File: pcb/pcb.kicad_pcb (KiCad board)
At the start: 2 copper layers, 165.5 x 101.1 mm, 59 parts, among them J1 N!N, J2 Conn_01x02_Socket, J4 Display_nice-view, J8 Conn_01x12_Socket, J9 Conn_01x12_Socket, SW1 Switch, SW10 Switch, SW11 Switch, SW12 Switch, SW13 Switch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

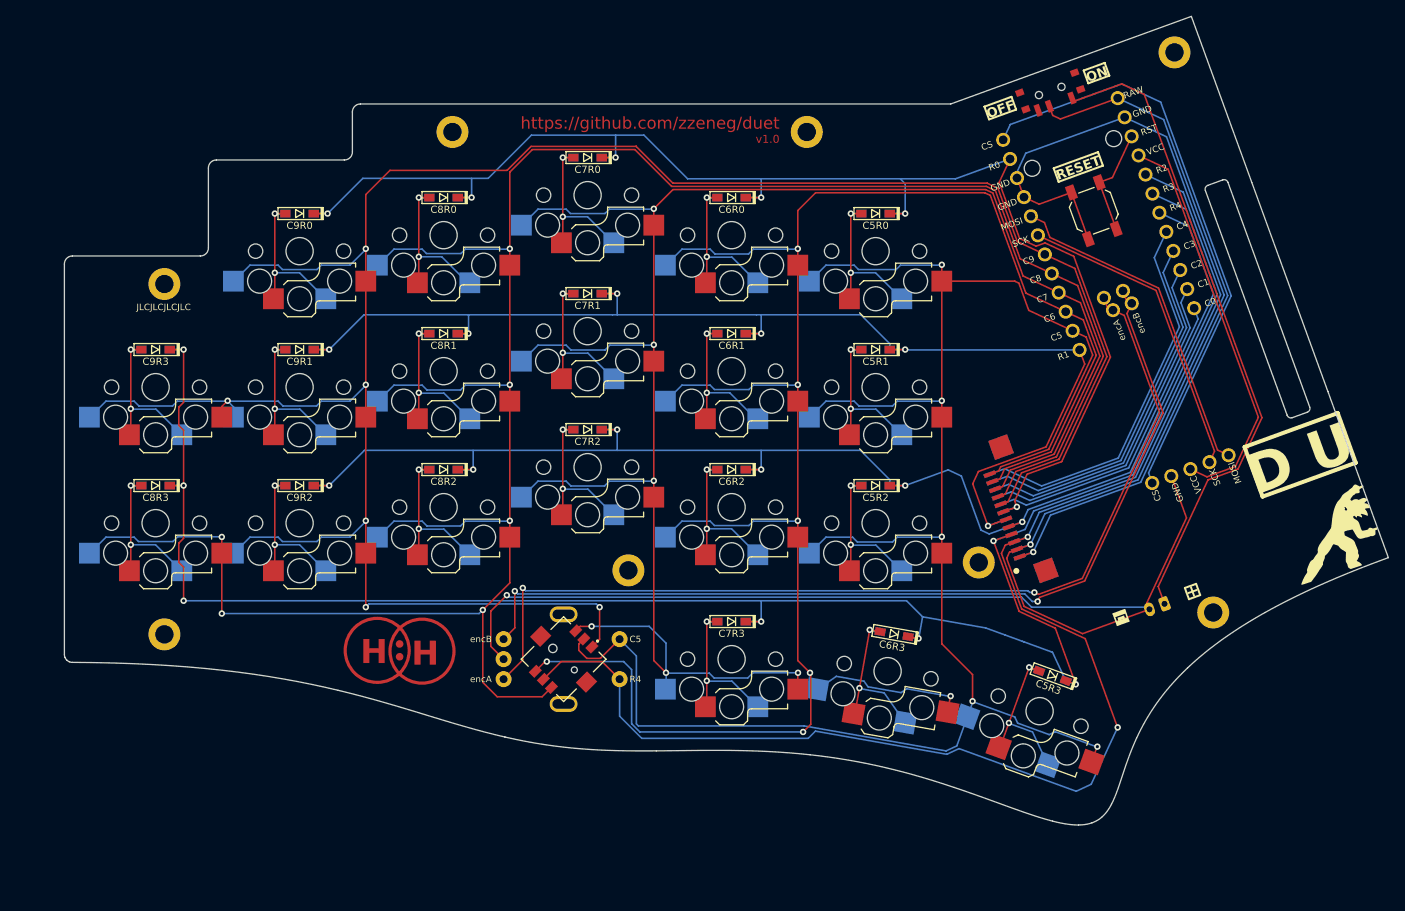
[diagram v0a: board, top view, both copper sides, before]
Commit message: converting duet to standard x and min y spacing, along with strong pinky stagger, WIP
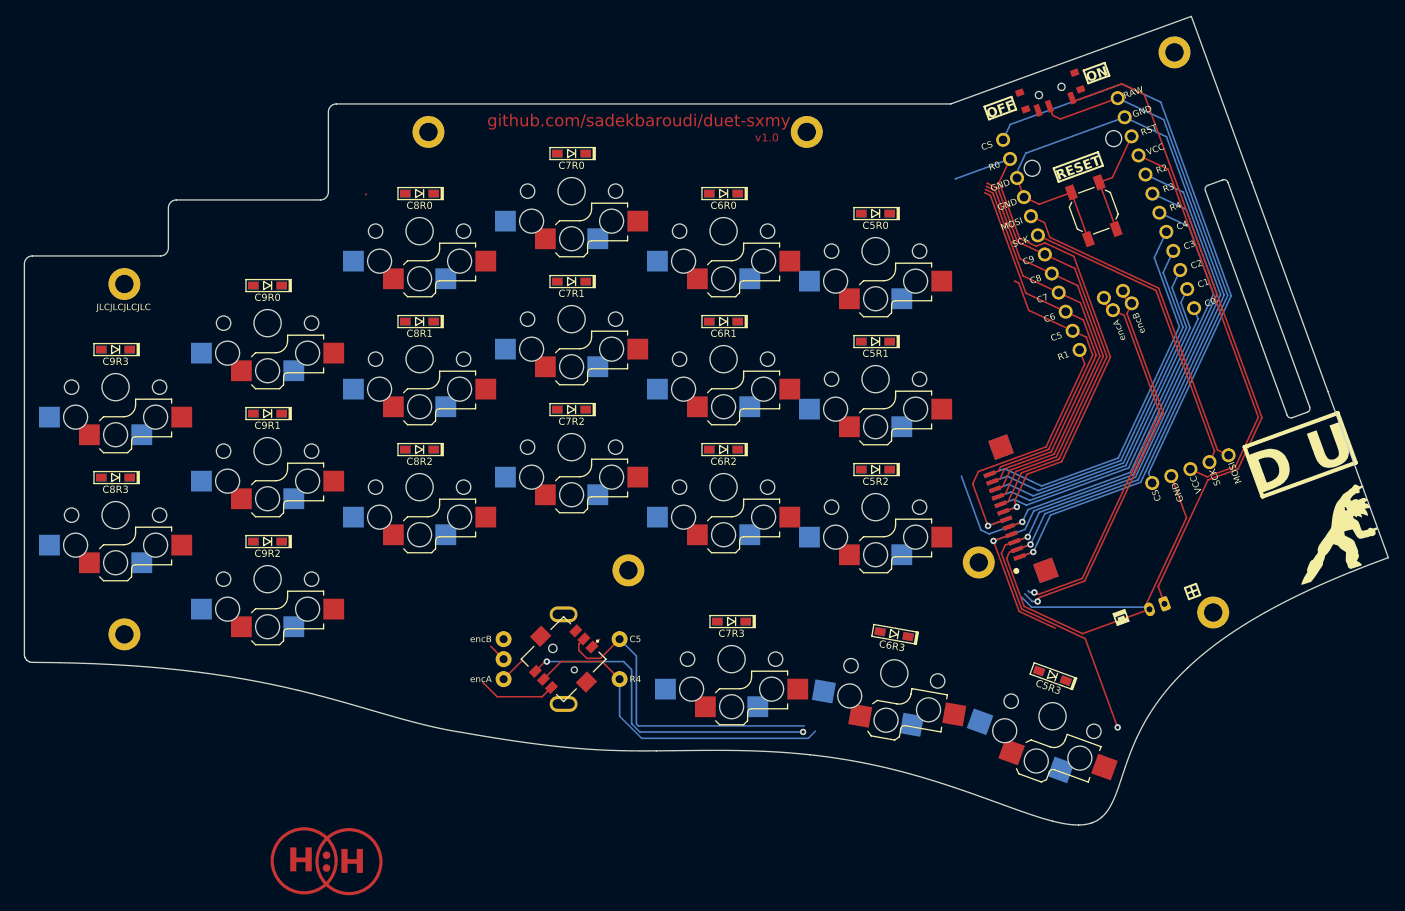
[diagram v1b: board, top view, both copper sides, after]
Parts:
- SW1, SW10, SW11, SW12, SW13, SW14, SW15, SW16, SW17, SW18, SW19, SW2, SW20, SW3, SW4, SW5, SW6, SW7, SW8, SW9: footprint zzkeeb:Switch_ChocV1-hotswap-reversible -> fingerpunch:Switch_ChocV1-hotswap-minY-reversible
- moved D1 9.85 mm to (61.5, 63.3)
- moved SW1 9.85 mm to (61.5, 68.0)
- moved D6 8.94 mm to (61.5, 79.3)
- moved SW6 8.94 mm to (61.5, 84.0)
- moved D11 8.06 mm to (61.5, 95.3)
- moved SW11 8.06 mm to (61.5, 100.0)
- moved D17 5.10 mm to (42.5, 87.3)
- moved SW17 5.10 mm to (42.5, 92.0)
- moved D16 5.00 mm to (42.5, 71.3)
- moved H1 5.00 mm to (43.6, 63.1)
- moved H5 5.00 mm to (43.6, 106.9)
- moved SW16 5.00 mm to (42.5, 76.0)
- moved D12 3.91 mm to (80.5, 83.8)
- moved SW12 3.91 mm to (80.5, 88.5)
- moved D7 3.35 mm to (80.5, 67.8)
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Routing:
- net col9: track 300.2 -> 53.8 mm, vias 6 -> 0
- net col8: track 302.5 -> 60.8 mm, vias 6 -> 0
- net col7: track 241.7 -> 49.7 mm, vias 6 -> 0
- net row3: track 253.0 -> 77.6 mm, vias 7 -> 1
- net col6: track 256.5 -> 89.9 mm, vias 7 -> 2
- net col5: track 240.3 -> 76.8 mm, vias 5 -> 0
- net row1: track 155.6 -> 34.4 mm, vias 6 -> 1
- net row0: track 180.7 -> 65.9 mm, vias 6 -> 1
- net row2: track 175.7 -> 67.5 mm, vias 6 -> 1
- net encA: track 122.4 -> 50.1 mm, vias 2 -> 1
- net GND: track 238.1 -> 166.5 mm, vias 2 -> 1
- net encB: track 118.9 -> 48.4 mm, vias 2 -> 1
- net row4: track 180.0 -> 136.1 mm
- net Net-(D3-A): track 21.2 -> 0.00 mm, vias 2 -> 0
- net Net-(D14-A): track 21.1 -> 0.00 mm, vias 2 -> 0
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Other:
- board size 165.5 x 101.1 mm -> 170.5 x 101.1 mm
- board text added: "-0.5"
- board text added: "10"
- board text added: "github.com/sadekbaroudi/duet-sxmy"
- board text removed: "https://github.com/zzeneg/duet"

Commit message: rerouted with the new layout, ready for production test
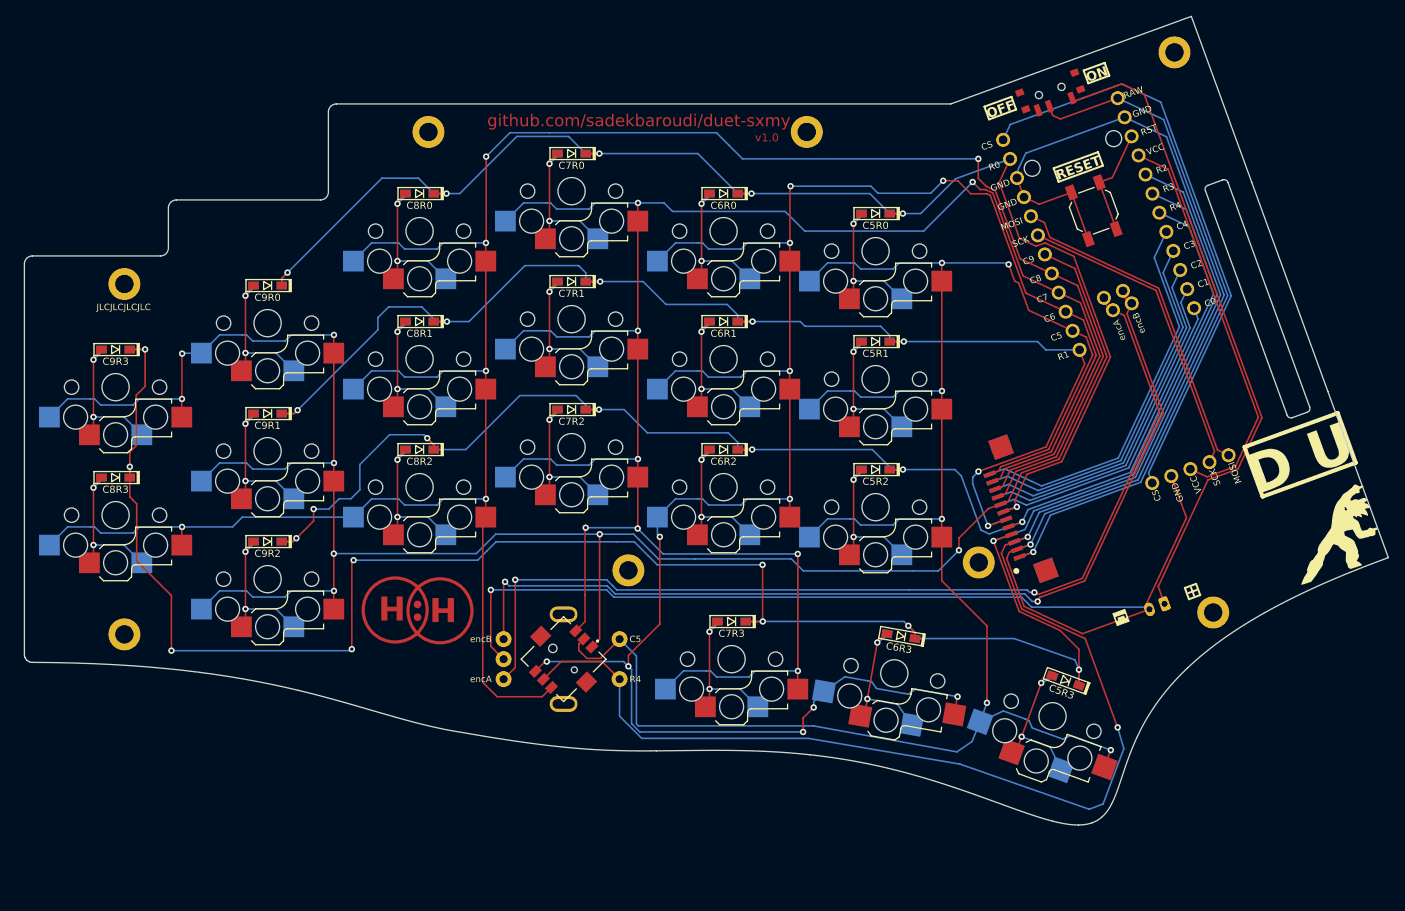
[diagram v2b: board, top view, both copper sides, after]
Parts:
- moved D20 1.75 mm to (161.3, 112.7)
- moved D19 0.90 mm to (140.7, 107.1)
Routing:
- net col8: track 60.8 -> 291.5 mm, vias 0 -> 6
- net col7: track 49.7 -> 269.1 mm, vias 0 -> 8
- net col9: track 53.8 -> 262.3 mm, vias 0 -> 8
- net row3: track 77.6 -> 276.4 mm, vias 1 -> 10
- net col5: track 76.8 -> 246.2 mm, vias 0 -> 6
- net col6: track 89.9 -> 258.7 mm, vias 2 -> 11
- net row1: track 34.4 -> 159.7 mm, vias 1 -> 7
- net row2: track 67.5 -> 178.6 mm, vias 1 -> 7
- net row0: track 65.9 -> 174.3 mm, vias 1 -> 6
- net encA: track 50.1 -> 124.4 mm, vias 1 -> 2
- net GND: track 166.5 -> 240.2 mm, vias 1 -> 2
- net encB: track 48.4 -> 121.3 mm, vias 1 -> 2
- net row4: track 136.1 -> 183.2 mm
- net Net-(D15-A): track 0.00 -> 19.9 mm, vias 0 -> 2
- net Net-(D9-A): track 0.00 -> 19.9 mm, vias 0 -> 2
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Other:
- board text removed: "-0.5"
- board text removed: "10"

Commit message: moved mounting hole, added updated dxfs, added sxmy cases, still need to do bottom plates
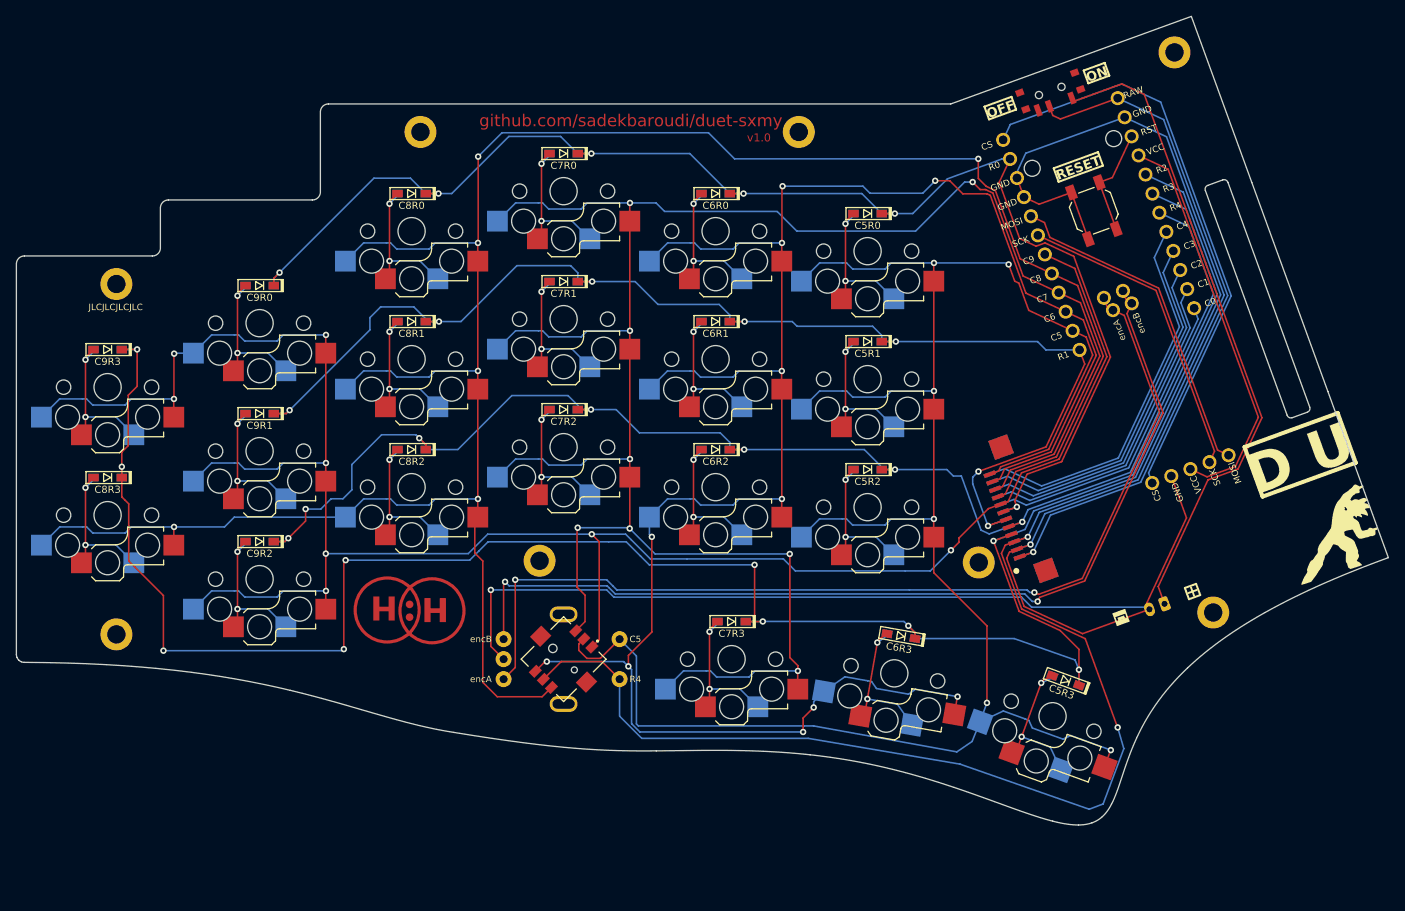
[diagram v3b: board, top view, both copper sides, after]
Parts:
- moved H6 12.2 mm to (94.5, 97.7)
- moved D1 1.00 mm to (60.5, 63.3)
- moved D10 1.00 mm to (136.5, 70.3)
- moved D11 1.00 mm to (60.5, 95.3)
- moved D12 1.00 mm to (79.5, 83.8)
- moved D13 1.00 mm to (98.5, 78.8)
- moved D14 1.00 mm to (117.5, 83.8)
- moved D15 1.00 mm to (136.5, 86.3)
- moved D16 1.00 mm to (41.5, 71.3)
- moved D17 1.00 mm to (41.5, 87.3)
- moved D2 1.00 mm to (79.5, 51.8)
- moved D3 1.00 mm to (98.5, 46.8)
- moved D4 1.00 mm to (117.5, 51.8)
- moved D5 1.00 mm to (136.5, 54.3)
- moved D6 1.00 mm to (60.5, 79.3)
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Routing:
- net col7: track 269.1 -> 270.9 mm
- net col8: track 291.5 -> 292.9 mm
- net col5: track 246.2 -> 247.6 mm
- net row0: track 174.3 -> 175.3 mm
- net row2: track 178.6 -> 179.6 mm
- net row1: track 159.7 -> 160.7 mm
- net col9: track 262.3 -> 263.0 mm
- net col6: track 258.7 -> 259.3 mm
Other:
- board size 170.5 x 101.1 mm -> 171.5 x 101.1 mm
